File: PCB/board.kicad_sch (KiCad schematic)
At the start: 169 parts, among them J1 Micro_SD_Card, J10 Conn_01x10, J11 Conn_01x02, J12 Conn_02x04_Odd_Even, J13 Conn_01x02, J14 Conn_01x02, J15 Conn_01x03, J16 Conn_01x02, J17 Conn_01x05, J18 Conn_01x04, J19 Conn_01x04, J2 Conn_ARM_JTAG_SWD_10, J20 Conn_01x02, J21 Conn_01x03, J22 Conn_02x04_Odd_Even, J23 Conn_01x04, J24 Conn_01x04, J25 Conn_01x02, J26 Conn_01x03, J27 Conn_02x04_Odd_Even, J28 Conn_01x04, J29 Conn_01x04, J30 Conn_01x02, J31 Conn_01x03, J32 Conn_01x02, J33 Conn_01x02, J34 Conn_01x02, J35 Conn_01x02, J36 Conn_01x02, J37 Conn_01x02, J4 Conn_01x04, J5 Conn_01x04, J6 Conn_01x02, J7 Conn_01x03, J8 Conn_02x04_Odd_Even, J9 Conn_01x10, P1 USB_C_Plug_USB2.0, Q1 IRLML6402, Q2 NMOS, Q3 NMOS, Q4 NMOS, Q5 NMOS, Q6 NMOS, SW1 SW_Push, SW2 SW_Push, U1 STM32H743VITx, U2 LDO, U3 TPS54331, U4 TMC Stepstick, U5 TMC Stepstick, U6 TMC Stepstick, U7 TMC Stepstick, Y1 25 MHz

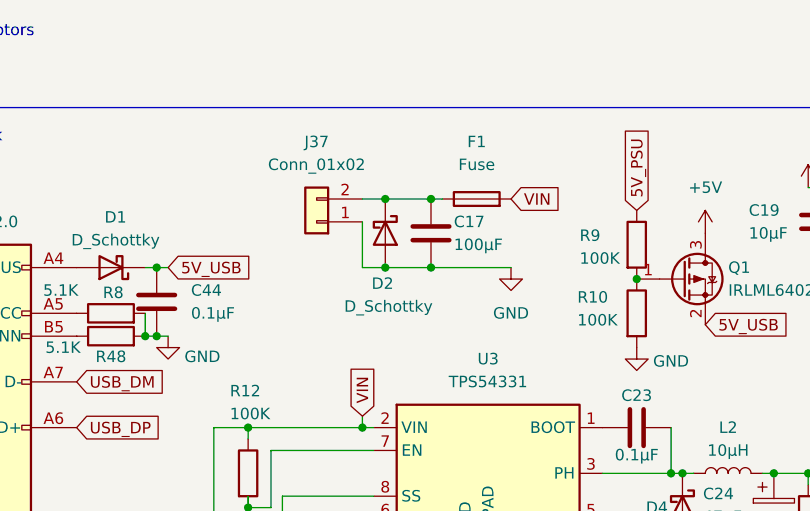
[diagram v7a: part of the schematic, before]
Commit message: moving the fuse before cap and diode
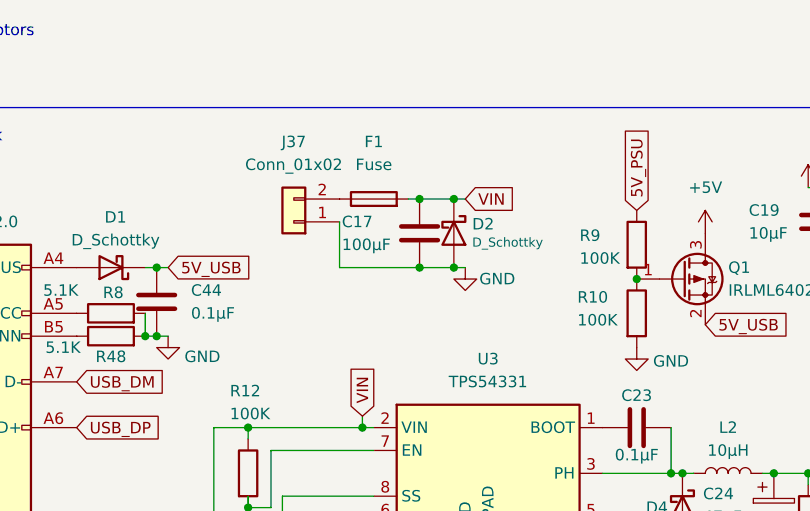
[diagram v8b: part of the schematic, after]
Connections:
- net VIN: now also C17.1, D2.1 (K)
- net at F1.1, J37.2 (Pin_2): no longer C17.1, D2.1 (K)
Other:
- moved on the sheet: C17, D2, F1, J37
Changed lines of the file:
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@@
 	)
 	(junction
+		(at 81.28 24.13)
+		(diameter 0)
+		(color 0 0 0 0)
+	)
+	(junction
+		(at 81.28 31.75)
+		(diameter 0)
+		(color 0 0 0 0)
+	)
+	(junction
 		(at 76.2 74.93)
 		(diameter 0)
@@
 	)
 	(junction
-		(at 77.47 24.13)
-		(diameter 0)
-		(color 0 0 0 0)
-	)
-	(junction
 		(at 33.02 190.5)
 		(diameter 0)
@@
 	)
 	(junction
-		(at 77.47 31.75)
-		(diameter 0)
-		(color 0 0 0 0)
-	)
-	(junction
 		(at 374.65 251.46)
 		(diameter 0)
@@
 	)
 	(junction
-		(at 82.55 24.13)
-		(diameter 0)
-		(color 0 0 0 0)
-	)
-	(junction
 		(at 71.12 74.93)
 		(diameter 0)
@@
 	)
 	(junction
+		(at 85.09 31.75)
+		(diameter 0)
+		(color 0 0 0 0)
+	)
+	(junction
 		(at 34.29 154.94)
 		(diameter 0)
@@
 	)
 	(junction
-		(at 82.55 31.75)
-		(diameter 0)
-		(color 0 0 0 0)
-	)
-	(junction
 		(at 33.02 198.12)
 		(diameter 0)
@@
 	)
 	(junction
+		(at 85.09 24.13)
+		(diameter 0)
+		(color 0 0 0 0)
+	)
+	(junction
 		(at 31.75 109.22)
 		(diameter 0)
@@
 	(wire
 		(pts
-			(xy 83.82 24.13) (xy 82.55 24.13)
-		)
-		(stroke
-			(width 0)
-			(type default)
-		)
-	)
-	(wire
-		(pts
 			(xy 257.81 27.94) (xy 264.16 27.94)
 		)
@@
 	(wire
 		(pts
+			(xy 81.28 31.75) (xy 85.09 31.75)
+		)
+		(stroke
+			(width 0)
+			(type default)
+		)
+	)
+	(wire
+		(pts
 			(xy 62.23 67.31) (xy 62.23 74.93)
 		)
@@
 	(wire
 		(pts
-			(xy 74.93 31.75) (xy 74.93 26.67)
+			(xy 72.39 31.75) (xy 72.39 26.67)
 		)
 		(stroke
@@
 	(wire
 		(pts
+			(xy 81.28 24.13) (xy 85.09 24.13)
+		)
+		(stroke
+			(width 0)
+			(type default)
+		)
+	)
+	(wire
+		(pts
 			(xy 374.65 49.53) (xy 378.46 49.53)
 		)
@@
 	(wire
 		(pts
-			(xy 77.47 24.13) (xy 82.55 24.13)
-		)
-		(stroke
-			(width 0)
-			(type default)
-		)
-	)
-	(wire
-		(pts
 			(xy 264.16 20.32) (xy 270.51 20.32)
 		)
@@
 	(wire
 		(pts
-			(xy 74.93 31.75) (xy 77.47 31.75)
+			(xy 72.39 31.75) (xy 81.28 31.75)
 		)
 		(stroke
@@
 	(wire
 		(pts
-			(xy 77.47 31.75) (xy 82.55 31.75)
-		)
-		(stroke
-			(width 0)
-			(type default)
-		)
-	)
-	(wire
-		(pts
 			(xy 66.04 67.31) (xy 66.04 74.93)
 		)
@@
 	(wire
 		(pts
+			(xy 85.09 24.13) (xy 86.36 24.13)
+		)
+		(stroke
+			(width 0)
+			(type default)
+		)
+	)
+	(wire
+		(pts
 			(xy 349.25 234.95) (xy 347.98 234.95)
 		)
@@
 	(wire
 		(pts
+			(xy 85.09 31.75) (xy 86.36 31.75)
+		)
+		(stroke
+			(width 0)
+			(type default)
+		)
+	)
+	(wire
+		(pts
 			(xy 20.32 69.85) (xy 24.13 69.85)
 		)
@@
 	(wire
 		(pts
+			(xy 80.01 24.13) (xy 81.28 24.13)
+		)
+		(stroke
+			(width 0)
+			(type default)
+		)
+	)
+	(wire
+		(pts
 			(xy 72.39 232.41) (xy 71.12 232.41)
 		)
@@
 	(wire
 		(pts
-			(xy 82.55 31.75) (xy 91.44 31.75)
-		)
-		(stroke
-			(width 0)
-			(type default)
-		)
-	)
-	(wire
-		(pts
 			(xy 66.04 74.93) (xy 71.12 74.93)
 		)
@@
 	(wire
 		(pts
-			(xy 74.93 24.13) (xy 77.47 24.13)
-		)
-		(stroke
-			(width 0)
-			(type default)
-		)
-	)
-	(wire
-		(pts
 			(xy 27.94 233.68) (xy 27.94 232.41)
 		)
@@
 	(global_label "VIN"
 		(shape input)
-		(at 91.44 24.13 0)
+		(at 86.36 24.13 0)
 		(fields_autoplaced yes)
 		(effects
@@
 		)
 		(property "Intersheetrefs" "${INTERSHEET_REFS}"
-			(at 97.4491 24.13 0)
+			(at 92.3691 24.13 0)
 			(effects
 				(font
@@
 	(symbol
 		(lib_id "Device:C")
-		(at 82.55 27.94 0)
+		(at 81.28 27.94 0)
 		(unit 1)
 		(exclude_from_sim no)
@@
 		(dnp no)
 		(property "Reference" "C17"
-			(at 85.09 26.67 0)
+			(at 72.644 26.67 0)
 			(effects
 				(font
@@
 		)
 		(property "Value" "100µF"
-			(at 85.09 29.21 0)
+			(at 72.644 29.21 0)
 			(effects
 				(font
@@
 		)
 		(property "Footprint" "Capacitor_THT:CP_Radial_D6.3mm_P2.50mm"
-			(at 83.5152 31.75 0)
+			(at 82.2452 31.75 0)
 			(effects
 				(font
@@
 		)
 		(property "Datasheet" "~"
-			(at 82.55 27.94 0)
+			(at 81.28 27.94 0)
 			(effects
 				(font
@@
 		)
 		(property "Description" "Unpolarized capacitor"
-			(at 82.55 27.94 0)
+			(at 81.28 27.94 0)
 			(effects
 				(font
@@
 		)
 		(instances
-			(project ""
+			(project "board"
 				(path "/93bdda59-fc0f-4b76-8be9-fa93964bed43"
 					(reference "C17")
@@
 	(symbol
 		(lib_id "Connector_Generic:Conn_01x02")
-		(at 69.85 26.67 180)
+		(at 67.31 26.67 180)
 		(unit 1)
 		(exclude_from_sim no)
@@
 		(fields_autoplaced yes)
 		(property "Reference" "J37"
-			(at 69.85 17.78 0)
+			(at 67.31 17.78 0)
 			(effects
 				(font
@@
 		)
 		(property "Value" "Conn_01x02"
-			(at 69.85 20.32 0)
+			(at 67.31 20.32 0)
 			(effects
 				(font
@@
 		)
 		(property "Footprint" "TerminalBlock_Phoenix:TerminalBlock_Phoenix_MKDS-1,5-2-5.08_1x02_P5.08mm_Horizontal"
-			(at 69.85 26.67 0)
+			(at 67.31 26.67 0)
 			(effects
 				(font
@@
 		)
 		(property "Datasheet" "~"
-			(at 69.85 26.67 0)
+			(at 67.31 26.67 0)
 			(effects
 				(font
@@
 		)
 		(property "Description" "Generic connector, single row, 01x02, script generated (kicad-library-utils/schlib/autogen/connector/)"
-			(at 69.85 26.67 0)
+			(at 67.31 26.67 0)
 			(effects
 				(font
@@
 	(symbol
 		(lib_id "Device:D_Schottky")
-		(at 77.47 27.94 270)
+		(at 85.09 27.94 270)
 		(unit 1)
 		(exclude_from_sim no)
@@
 		(dnp no)
 		(property "Reference" "D2"
-			(at 75.946 33.528 90)
+			(at 87.122 26.924 90)
 			(effects
 				(font
@@
 		)
 		(property "Value" "D_Schottky"
-			(at 72.898 36.068 90)
+			(at 87.122 28.956 90)
 			(effects
 				(font
-					(size 1.27 1.27)
+					(size 1.016 1.016)
 				)
 				(justify left)
@@
 		)
 		(property "Footprint" "Package_TO_SOT_THT:TO-220-2_Vertical"
-			(at 77.47 27.94 0)
+			(at 85.09 27.94 0)
 			(effects
 				(font
@@
 		)
 		(property "Datasheet" "~"
-			(at 77.47 27.94 0)
+			(at 85.09 27.94 0)
 			(effects
 				(font
@@
 		)
 		(property "Description" "Schottky diode"
-			(at 77.47 27.94 0)
+			(at 85.09 27.94 0)
 			(effects
 				(font
@@
 		)
 		(instances
-			(project ""
+			(project "board"
 				(path "/93bdda59-fc0f-4b76-8be9-fa93964bed43"
 					(reference "D2")
@@
 	(symbol
 		(lib_id "Device:Fuse")
-		(at 87.63 24.13 90)
+		(at 76.2 24.13 90)
 		(unit 1)
 		(exclude_from_sim no)
@@
 		(fields_autoplaced yes)
 		(property "Reference" "F1"
-			(at 87.63 17.78 90)
+			(at 76.2 17.78 90)
 			(effects
 				(font
@@
 		)
 		(property "Value" "Fuse"
-			(at 87.63 20.32 90)
+			(at 76.2 20.32 90)
 			(effects
 				(font
@@
 		)
 		(property "Footprint" "Fuse:Fuse_Blade_Mini_directSolder"
-			(at 87.63 25.908 90)
+			(at 76.2 25.908 90)
 			(effects
 				(font
@@
 		)
 		(property "Datasheet" "~"
-			(at 87.63 24.13 0)
+			(at 76.2 24.13 0)
 			(effects
 				(font
@@
 		)
 		(property "Description" "Fuse"
-			(at 87.63 24.13 0)
+			(at 76.2 24.13 0)
 			(effects
 				(font
@@
 	(symbol
 		(lib_id "power:GND")
-		(at 91.44 31.75 0)
+		(at 86.36 31.75 0)
 		(unit 1)
 		(exclude_from_sim no)
@@
 		(on_board yes)
 		(dnp no)
-		(fields_autoplaced yes)
 		(property "Reference" "#PWR016"
-			(at 91.44 38.1 0)
+			(at 86.36 38.1 0)
 			(effects
 				(font
@@
 		)
 		(property "Value" "GND"
-			(at 91.44 36.83 0)
+			(at 89.916 33.02 0)
 			(effects
 				(font
@@
 		)
 		(property "Footprint" ""
-			(at 91.44 31.75 0)
+			(at 86.36 31.75 0)
 			(effects
 				(font
@@
 		)
 		(property "Datasheet" ""
-			(at 91.44 31.75 0)
+			(at 86.36 31.75 0)
 			(effects
 				(font
@@
 		)
 		(property "Description" "Power symbol creates a global label with name \"GND\" , ground"
-			(at 91.44 31.75 0)
+			(at 86.36 31.75 0)
 			(effects
 				(font
